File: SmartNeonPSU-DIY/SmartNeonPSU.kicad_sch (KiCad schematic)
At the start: 77 parts, among them J1 POWER, J2 POWER, J3 SERIAL+GPIO, J4 TPS_IO, J5 LAMP1+, J6 LAMP1-, Q1 IRF7303, Q2 IRF7303, Q3 MMSS8050, Q4 MMSS8050, SW1 RESET, SW2 BOOT/IO0, SW3 CONTROL, U1 AP2205-33Y, U2 TPS68000, U3 ESP32-WROOM-32D

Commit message: v1
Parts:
- removed JP1: TPS_VCC, Jumper:SolderJumper-3_P1.3mm_Bridged12_RoundedPad1.0x1.5mm, symbol Jumper:SolderJumper_3_Open
- added D5: FAULT, LED_SMD:LED_0805_2012Metric, symbol Device:LED
- added J5: EXT_SW, Connector_PinSocket_2.54mm:PinSocket_1x03_P2.54mm_Vertical, symbol Connector_Generic:Conn_01x03
- added R17: 1K, Resistor_SMD:R_0805_2012Metric, symbol Device:R
- added R6, R7, R8, R9: 10K, Resistor_SMD:R_0805_2012Metric, symbol Device:R
- C1: footprint Capacitor_SMD:CP_Elec_5x5.3 -> Capacitor_SMD:CP_Elec_8x6.9
- H1, H2, H3, H4, H5: footprint MountingHole:MountingHole_2.2mm_M2_Pad_Via -> MountingHole:MountingHole_3.2mm_M3_Pad_Via
- J1: value POWER -> 12VDC
- RV2: Population (none) -> DNP
- SW2: value BOOT/IO0 -> IO0
- TR1: MPN1 B66206J1106T001 -> (none)
- renumbered C15 to C14, C16 to C15, C14 to C16, J5 to J6, J6 to J7, Q3 to Q1, Q4 to Q2, Q1 to Q3, Q2 to Q4, R6 to R10, R7 to R11, R8 to R12, R9 to R13, R10 to R14, R11 to R15, R12 to R16, R15 to R18, R16 to R19, R13 to R20, R14 to R21, R17 to R22, R18 to R23, R19 to R24, R20 to R25
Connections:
- net GPIO25 is gone; now on net BC: U3.10 (IO25)
- net TPS_VCC is gone; now on net +12V: C10.1, U2.24 (VCC)
- net +3V3: now also R17.1
- net ABR: now also R6.1, R7.2
- net BBR: now also R8.1, R9.2
- net BC: no longer U3.12 (IO27)
- net FAULT: now also D5.1 (K)
- net GND: now also RV1.1, RV2.1, J5.2 (Pin_2), R7.1, R9.1; no longer RV1.3, RV2.3
- net GPIO0: now also J5.1 (Pin_1)
- net GPIO2: now also J5.3 (Pin_3)
- net V5: now also RV2.3, R8.2; no longer RV2.1
- net VREF: now also RV1.3, R6.2; no longer RV1.1
- new net: D5.2 (A), R17.2
- new net GPIO27: U3.12 (IO27)
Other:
- note added: "External Switch"
- moved on the sheet: C16, C17, C18, C3, Q1, Q2, R18, R19, R20, R21, R22, RV1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

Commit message: v2
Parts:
- added C5: 1 uF, Capacitor_SMD:C_0805_2012Metric, symbol Device:C
- added JP1: ESP-ABR, Jumper:SolderJumper-2_P1.3mm_Bridged_RoundedPad1.0x1.5mm, symbol Jumper:SolderJumper_2_Bridged
- added JP2: ESP-BC, Jumper:SolderJumper-2_P1.3mm_Bridged_RoundedPad1.0x1.5mm, symbol Jumper:SolderJumper_2_Bridged
- added U1: TSOP382xx, OptoDevice:Vishay_MINICAST-3Pin, symbol Interface_Optical:TSOP382xx
- renumbered C9 to C10, C10 to C11, C11 to C12, C12 to C13, C13 to C14, C14 to C15, C15 to C16, C16 to C17, C17 to C18, C18 to C19, C19 to C20, C20 to C21, C21 to C22, C5 to C6, C6 to C7, C7 to C8, C8 to C9, U1 to U2, U2 to U3, U3 to U4
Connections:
- net GPIO27 is gone; now on net TPS_EN: U4.12 (IO27)
- net +3V3: now also C5.2, U1.3 (Vs)
- net ABR: now also JP1.2 (B)
- net BC: now also JP2.2 (B); no longer U4.10 (IO25)
- net GND: now also C5.1, U1.2 (GND)
- net GPI35: now also U1.1 (OUT)
- net TPS_EN: no longer U4.11 (IO26)
- new net ESP_ABR: JP1.1 (A), U4.10 (IO25)
- new net ESP_BC: JP2.1 (A), U4.11 (IO26)

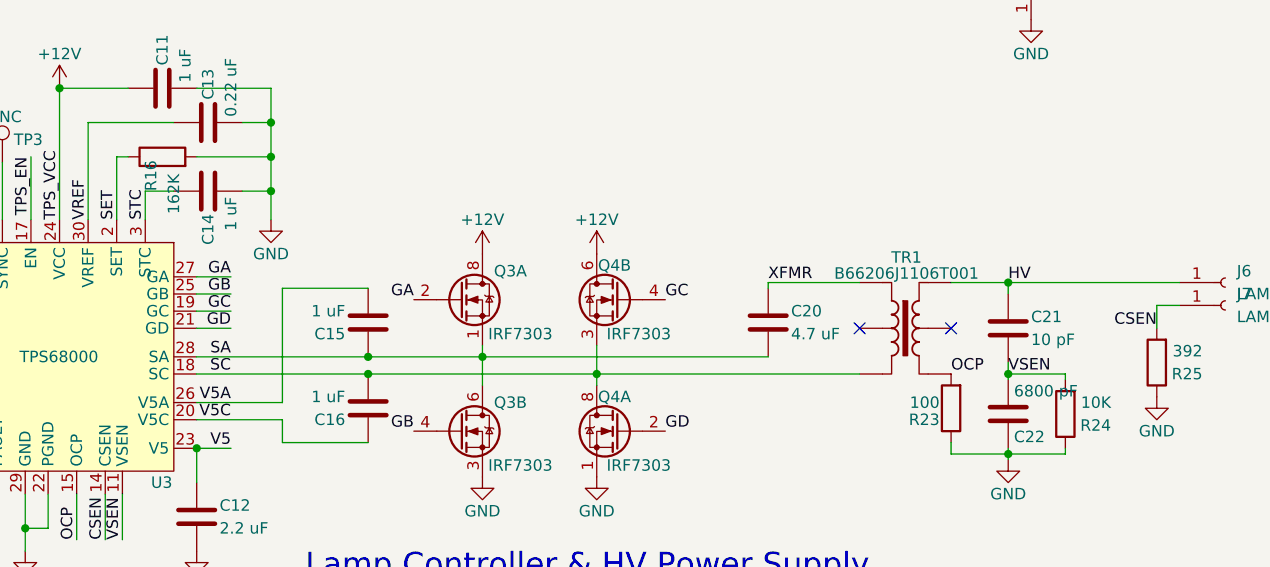
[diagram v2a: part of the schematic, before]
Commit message: Add docs, sync schematics with reality
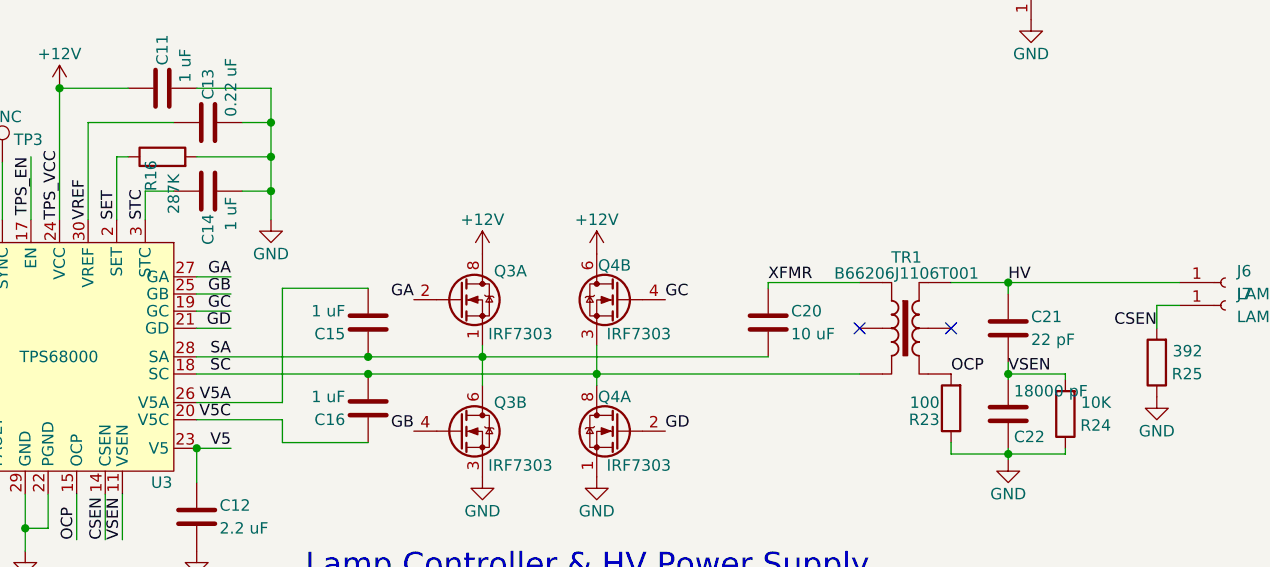
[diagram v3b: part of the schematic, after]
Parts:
- C20: value 4.7 uF -> 10 uF; MPN1 C2012X7R1H475K125AE -> C2012X5R1V106K085AC
- C21: value 10 pF -> 22 pF; MPN1 C4520C0G3F100F -> C4520C0G3F220K
- C22: value 6800 pF -> 18000 pF; MPN1 CC0805KRX7R9BB682 -> CC0805KRX7R9BB183
- R16: value 162K -> 287K; MPN1 RC0805FR-07162KL -> RC0805FR-07287KL
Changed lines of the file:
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@@
       (effects (font (size 1.27 1.27)) (justify left))
     )
-    (property "Value" "10 pF" (id 1) (at 253.365 133.35 0)
+    (property "Value" "22 pF" (id 1) (at 253.365 133.35 0)
       (effects (font (size 1.27 1.27)) (justify left))
     )
@@
       (effects (font (size 1.27 1.27)) hide)
     )
-    (property "MPN1" "C4520C0G3F100F" (id 4) (at 250.825 132.08 0)
+    (property "MPN1" "C4520C0G3F220K" (id 4) (at 250.825 132.08 0)
       (effects (font (size 1.27 1.27)) hide)
     )
@@
       (effects (font (size 1.27 1.27)) (justify left))
     )
-    (property "Value" "6800 pF" (id 1) (at 251.46 139.065 0)
+    (property "Value" "18000 pF" (id 1) (at 251.46 139.065 0)
       (effects (font (size 1.27 1.27)) (justify left))
     )
@@
       (effects (font (size 1.27 1.27)) hide)
     )
-    (property "MPN1" "CC0805KRX7R9BB682" (id 4) (at 250.825 141.605 0)
+    (property "MPN1" "CC0805KRX7R9BB183" (id 4) (at 250.825 141.605 0)
       (effects (font (size 1.27 1.27)) hide)
     )
@@
       (effects (font (size 1.27 1.27)) (justify left))
     )
-    (property "Value" "162K" (id 1) (at 158.115 119.38 0)
+    (property "Value" "287K" (id 1) (at 158.115 119.38 0)
       (effects (font (size 1.27 1.27)) (justify left))
     )
@@
       (effects (font (size 1.27 1.27)) hide)
     )
-    (property "MPN1" "RC0805FR-07162KL" (id 4) (at 156.845 113.03 0)
+    (property "MPN1" "RC0805FR-07287KL" (id 4) (at 156.845 113.03 0)
       (effects (font (size 1.27 1.27)) hide)
     )
@@
     )
     (pin "1")
-  )
-  (symbol (lib_id "Device:C") (at 224.155 131.445 0) (unit 1)
-    (in_bom yes) (on_board yes)
-    (property "Reference" "C20" (id 0) (at 226.695 130.175 0)
-      (effects (font (size 1.27 1.27)) (justify left))
-    )
-    (property "Value" "4.7 uF" (id 1) (at 226.695 132.715 0)
-      (effects (font (size 1.27 1.27)) (justify left))
-    )
-    (property "Footprint" "Capacitor_SMD:C_0805_2012Metric" (id 2) (at 225.1202 135.255 0)
-      (effects (font (size 1.27 1.27)) hide)
-    )
-    (property "Datasheet" "~" (id 3) (at 224.155 131.445 0)
-      (effects (font (size 1.27 1.27)) hide)
-    )
-    (property "MPN1" "C2012X7R1H475K125AE" (id 4) (at 224.155 131.445 0)
-      (effects (font (size 1.27 1.27)) hide)
-    )
-    (pin "1")
-    (pin "2")
   )
   (symbol (lib_id "Device:R") (at 71.628 139.7144 180) (unit 1)
@@
     (pin "7")
     (pin "8")
+  )
+  (symbol (lib_id "Device:C") (at 224.155 131.445 0) (unit 1)
+    (in_bom yes) (on_board yes)
+    (property "Reference" "C20" (id 0) (at 226.695 130.175 0)
+      (effects (font (size 1.27 1.27)) (justify left))
+    )
+    (property "Value" "10 uF" (id 1) (at 226.695 132.715 0)
+      (effects (font (size 1.27 1.27)) (justify left))
+    )
+    (property "Footprint" "Capacitor_SMD:C_0805_2012Metric" (id 2) (at 225.1202 135.255 0)
+      (effects (font (size 1.27 1.27)) hide)
+    )
+    (property "Datasheet" "~" (id 3) (at 224.155 131.445 0)
+      (effects (font (size 1.27 1.27)) hide)
+    )
+    (property "MPN1" "C2012X5R1V106K085AC" (id 4) (at 224.155 131.445 0)
+      (effects (font (size 1.27 1.27)) hide)
+    )
+    (pin "1")
+    (pin "2")
   )
   (symbol (lib_id "Device:R") (at 179.07 82.55 270) (unit 1)
@@
       (reference "C19") (unit 1) (value "47 uF") (footprint "Capacitor_SMD:C_0805_2012Metric")
     )
-    (path "/aa213ca8-3e06-4412-af52-3386c4fab9f9"
-      (reference "C20") (unit 1) (value "4.7 uF") (footprint "Capacitor_SMD:C_0805_2012Metric")
+    (path "/b1eb1033-7db7-4a8a-899a-17c54dd71492"
+      (reference "C20") (unit 1) (value "10 uF") (footprint "Capacitor_SMD:C_0805_2012Metric")
     )
     (path "/449e3155-16ea-42e5-8b6a-0c318fc89476"
-      (reference "C21") (unit 1) (value "10 pF") (footprint "Capacitor_SMD:C_1808_4520Metric_Slot")
+      (reference "C21") (unit 1) (value "22 pF") (footprint "Capacitor_SMD:C_1808_4520Metric_Slot")
     )
     (path "/51b8c561-e459-4fac-a380-3761f1257871"
-      (reference "C22") (unit 1) (value "6800 pF") (footprint "Capacitor_SMD:C_0805_2012Metric")
+      (reference "C22") (unit 1) (value "18000 pF") (footprint "Capacitor_SMD:C_0805_2012Metric")
     )
     (path "/bc1c377b-a155-474a-a038-dbd44a4e7dd6"
@@
     )
     (path "/9a45920d-217a-4a92-b6c2-ecc141d16559"
-      (reference "R16") (unit 1) (value "162K") (footprint "Resistor_SMD:R_0805_2012Metric")
+      (reference "R16") (unit 1) (value "287K") (footprint "Resistor_SMD:R_0805_2012Metric")
     )
     (path "/097b057b-6f92-4820-a5b5-7281e3dc927b"
